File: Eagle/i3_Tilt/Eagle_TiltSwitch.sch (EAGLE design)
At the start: 5 parts, among them J1 TILT

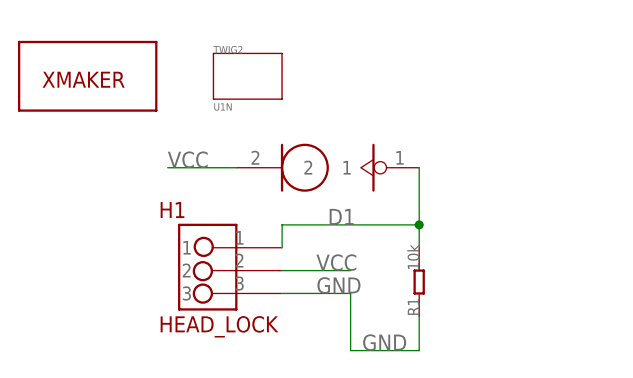
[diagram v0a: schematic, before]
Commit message: 调整蜂鸣器
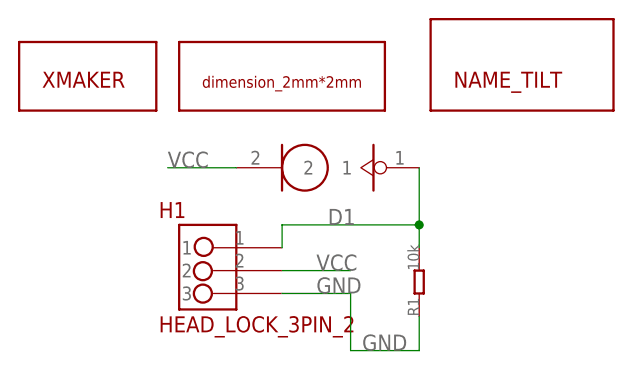
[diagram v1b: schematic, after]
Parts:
- removed TWIG2: U1N, twig_template1:U1N
- added U$3: DIMENSION_2MM2MM, Xmaker:DIMENSION_2MM2MM
- added U$4: NAME_LILT, Xmaker:NAME_LILT
- H1: value HEAD_LOCK -> HEAD_LOCK_3PIN_2; device HEAD_LOCK:HEAD_LOCK -> Xmaker:HEAD_LOCK_3PIN_2
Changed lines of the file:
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@@
 <?xml version="1.0" encoding="utf-8"?>
 <!DOCTYPE eagle SYSTEM "eagle.dtd">
-<eagle version="6.6.0">
+<eagle version="7.2.0">
 <drawing>
 <settings>
@@
 <layer number="54" name="bGND_GNDA" color="1" fill="9" visible="no" active="no"/>
 <layer number="56" name="wert" color="7" fill="1" visible="no" active="no"/>
+<layer number="57" name="tCAD" color="7" fill="1" visible="no" active="no"/>
+<layer number="59" name="tCarbon" color="7" fill="1" visible="no" active="no"/>
+<layer number="60" name="bCarbon" color="7" fill="1" visible="no" active="no"/>
+<layer number="90" name="Modules" color="5" fill="1" visible="no" active="no"/>
 <layer number="91" name="Nets" color="2" fill="1" visible="yes" active="yes"/>
 <layer number="92" name="Busses" color="1" fill="1" visible="yes" active="yes"/>
@@
 <layer number="97" name="Info" color="7" fill="1" visible="yes" active="yes"/>
 <layer number="98" name="Guide" color="6" fill="1" visible="yes" active="yes"/>
+<layer number="99" name="SpiceOrder" color="7" fill="1" visible="no" active="no"/>
 <layer number="100" name="Muster" color="7" fill="1" visible="no" active="no"/>
 <layer number="101" name="Patch_Top" color="12" fill="4" visible="yes" active="yes"/>
 <layer number="102" name="Vscore" color="7" fill="1" visible="yes" active="yes"/>
+<layer number="103" name="tMap" color="7" fill="1" visible="yes" active="yes"/>
 <layer number="104" name="Name" color="7" fill="1" visible="yes" active="yes"/>
+<layer number="105" name="tPlate" color="7" fill="1" visible="yes" active="yes"/>
+<layer number="106" name="bPlate" color="7" fill="1" visible="yes" active="yes"/>
+<layer number="107" name="Crop" color="7" fill="1" visible="yes" active="yes"/>
+<layer number="108" name="fp8" color="7" fill="1" visible="yes" active="yes"/>
+<layer number="109" name="fp9" color="7" fill="1" visible="yes" active="yes"/>
+<layer number="110" name="110" color="7" fill="1" visible="yes" active="yes"/>
+<layer number="111" name="111" color="7" fill="1" visible="yes" active="yes"/>
+<layer number="112" name="tSilk" color="7" fill="1" visible="yes" active="yes"/>
+<layer number="113" name="IDFDebug" color="7" fill="1" visible="yes" active="yes"/>
 <layer number="116" name="Patch_BOT" color="9" fill="4" visible="yes" active="yes"/>
+<layer number="118" name="Rect_Pads" color="7" fill="1" visible="yes" active="yes"/>
 <layer number="121" name="_tsilk" color="7" fill="1" visible="yes" active="yes"/>
 <layer number="122" name="_bsilk" color="7" fill="1" visible="yes" active="yes"/>
+<layer number="123" name="tTestmark" color="7" fill="1" visible="yes" active="yes"/>
+<layer number="124" name="bTestmark" color="7" fill="1" visible="yes" active="yes"/>
+<layer number="125" name="_tNames" color="7" fill="1" visible="yes" active="yes"/>
+<layer number="126" name="_bNames" color="7" fill="1" visible="yes" active="yes"/>
+<layer number="127" name="_tValues" color="7" fill="1" visible="yes" active="yes"/>
+<layer number="128" name="_bValues" color="7" fill="1" visible="yes" active="yes"/>
+<layer number="129" name="Mask" color="7" fill="1" visible="yes" active="yes"/>
+<layer number="131" name="tAdjust" color="7" fill="1" visible="yes" active="yes"/>
+<layer number="132" name="bAdjust" color="7" fill="1" visible="yes" active="yes"/>
+<layer number="144" name="DrillLegend" color="7" fill="1" visible="yes" active="yes"/>
+<layer number="150" name="Notes" color="7" fill="1" visible="yes" active="yes"/>
 <layer number="151" name="HeatSink" color="7" fill="1" visible="yes" active="yes"/>
+<layer number="152" name="_bDocu" color="7" fill="1" visible="yes" active="yes"/>
+<layer number="153" name="FabDoc1" color="7" fill="1" visible="yes" active="yes"/>
+<layer number="154" name="FabDoc2" color="7" fill="1" visible="yes" active="yes"/>
+<layer number="155" name="FabDoc3" color="7" fill="1" visible="yes" active="yes"/>
+<layer number="199" name="Contour" color="7" fill="1" visible="yes" active="yes"/>
 <layer number="200" name="200bmp" color="1" fill="10" visible="no" active="no"/>
 <layer number="201" name="201bmp" color="2" fill="1" visible="no" active="no"/>
@@
 <layer number="207" name="207bmp" color="8" fill="10" visible="no" active="yes"/>
 <layer number="208" name="208bmp" color="9" fill="10" visible="no" active="yes"/>
+<layer number="209" name="209bmp" color="7" fill="1" visible="yes" active="yes"/>
+<layer number="210" name="210bmp" color="7" fill="1" visible="yes" active="yes"/>
+<layer number="211" name="211bmp" color="7" fill="1" visible="yes" active="yes"/>
+<layer number="212" name="212bmp" color="7" fill="1" visible="yes" active="yes"/>
+<layer number="213" name="213bmp" color="7" fill="1" visible="yes" active="yes"/>
+<layer number="214" name="214bmp" color="7" fill="1" visible="yes" active="yes"/>
+<layer number="215" name="215bmp" color="7" fill="1" visible="yes" active="yes"/>
+<layer number="216" name="216bmp" color="7" fill="1" visible="yes" active="yes"/>
+<layer number="217" name="217bmp" color="7" fill="1" visible="yes" active="yes"/>
+<layer number="218" name="218bmp" color="7" fill="1" visible="yes" active="yes"/>
+<layer number="219" name="219bmp" color="7" fill="1" visible="yes" active="yes"/>
+<layer number="220" name="220bmp" color="7" fill="1" visible="yes" active="yes"/>
+<layer number="221" name="221bmp" color="7" fill="1" visible="yes" active="yes"/>
+<layer number="222" name="222bmp" color="7" fill="1" visible="yes" active="yes"/>
+<layer number="223" name="223bmp" color="7" fill="1" visible="yes" active="yes"/>
+<layer number="224" name="224bmp" color="7" fill="1" visible="yes" active="yes"/>
+<layer number="225" name="225bmp" color="7" fill="1" visible="yes" active="yes"/>
+<layer number="226" name="226bmp" color="7" fill="1" visible="yes" active="yes"/>
+<layer number="227" name="227bmp" color="7" fill="1" visible="yes" active="yes"/>
+<layer number="228" name="228bmp" color="7" fill="1" visible="yes" active="yes"/>
+<layer number="229" name="229bmp" color="7" fill="1" visible="yes" active="yes"/>
+<layer number="230" name="230bmp" color="7" fill="1" visible="yes" active="yes"/>
+<layer number="231" name="231bmp" color="7" fill="1" visible="yes" active="yes"/>
+<layer number="248" name="Housing" color="7" fill="1" visible="yes" active="yes"/>
+<layer number="249" name="Edge" color="7" fill="1" visible="yes" active="yes"/>
 <layer number="250" name="Descript" color="3" fill="1" visible="no" active="no"/>
 <layer number="251" name="SMDround" color="12" fill="11" visible="no" active="no"/>
 <layer number="254" name="cooling" color="7" fill="1" visible="yes" active="yes"/>
+<layer number="255" name="routoute" color="7" fill="1" visible="yes" active="yes"/>
 </layers>
 <schematic xreflabel="%F%N/%S.%C%R" xrefpart="/%S.%C%R">
@@
 <part name="R1" library="Discrete" deviceset="005-R*" device="0603" value="10k"/>
 <part name="J1" library="Seeed" deviceset="TILT" device=""/>
-<part name="TWIG2" library="twig_template1" deviceset="U1N" device=""/>
-<part name="H1" library="HEAD_LOCK" deviceset="HEAD_LOCK" device=""/>
+<part name="H1" library="Xmaker" deviceset="HEAD_LOCK_3PIN_2" device=""/>
 <part name="U$2" library="Xmaker_yuhui" deviceset="XMAKERLOGO" device=""/>
+<part name="U$3" library="Xmaker" deviceset="DIMENSION_2MM*2MM" device=""/>
+<part name="U$4" library="Xmaker" deviceset="NAME_LILT" device=""/>
 </parts>
 <sheets>
@@
 <instance part="R1" gate="R" x="64.77" y="34.29" rot="R90"/>
 <instance part="J1" gate="G$1" x="54.61" y="46.99" rot="R270"/>
-<instance part="TWIG2" gate="G$1" x="45.72" y="57.15"/>
-<instance part="H1" gate="G$1" x="36.83" y="27.94"/>
+<instance part="H1" gate="G$1" x="41.91" y="35.56"/>
 <instance part="U$2" gate="G$1" x="27.94" y="55.88"/>
+<instance part="U$3" gate="G$1" x="38.1" y="53.34"/>
+<instance part="U$4" gate="G$1" x="76.2" y="58.42"/>
 </instances>
 <busses>
